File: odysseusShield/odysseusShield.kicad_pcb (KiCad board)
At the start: 2 copper layers, 53.3 x 49.5 mm, 6 parts, among them J1 Conn_01x32, J2 Conn_01x07, Q1 SSM3K333R, Q2 SSM3K333R

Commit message: working on adding logo to PCB, edited PCB based on joystick and fan additions
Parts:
- added J3: Conn_01x07, odysseusWindows:Header_P2.54mm_7, F.Cu at (156.2, 106.7)
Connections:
- J1 pad 22: Net-(J1-Pad22) -> /Joy3
- J1 pad 23: Net-(J1-Pad23) -> /Joy2
- J1 pad 24: Net-(J1-Pad24) -> /Joy1
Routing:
- net /Joy1: track 0.00 -> 43.3 mm
- net /Joy3: track 0.00 -> 41.1 mm
- net /Joy2: track 0.00 -> 40.1 mm
- net +12V: track 22.4 -> 39.7 mm
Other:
- net class Default: clearance 0.254 -> 0.1524; via_dia 0.6 -> 0.6096; via_drill 0.4 -> 0.3048
- rule trace_clearance: 0.254 -> 0.1524
- rule trace_min: 0.2 -> 0.254
- rule via_min_drill: 0.3 -> 0.3048
- rule via_min_size: 0.4 -> 0.6096
- board text added: "Alex Chapman Anil Patel Lucky Jordan (PCB Designer) Nathan Lepore Sean Szymanski Odysseus Shield V1 11/17/2017 Olin College of Engineering POE"

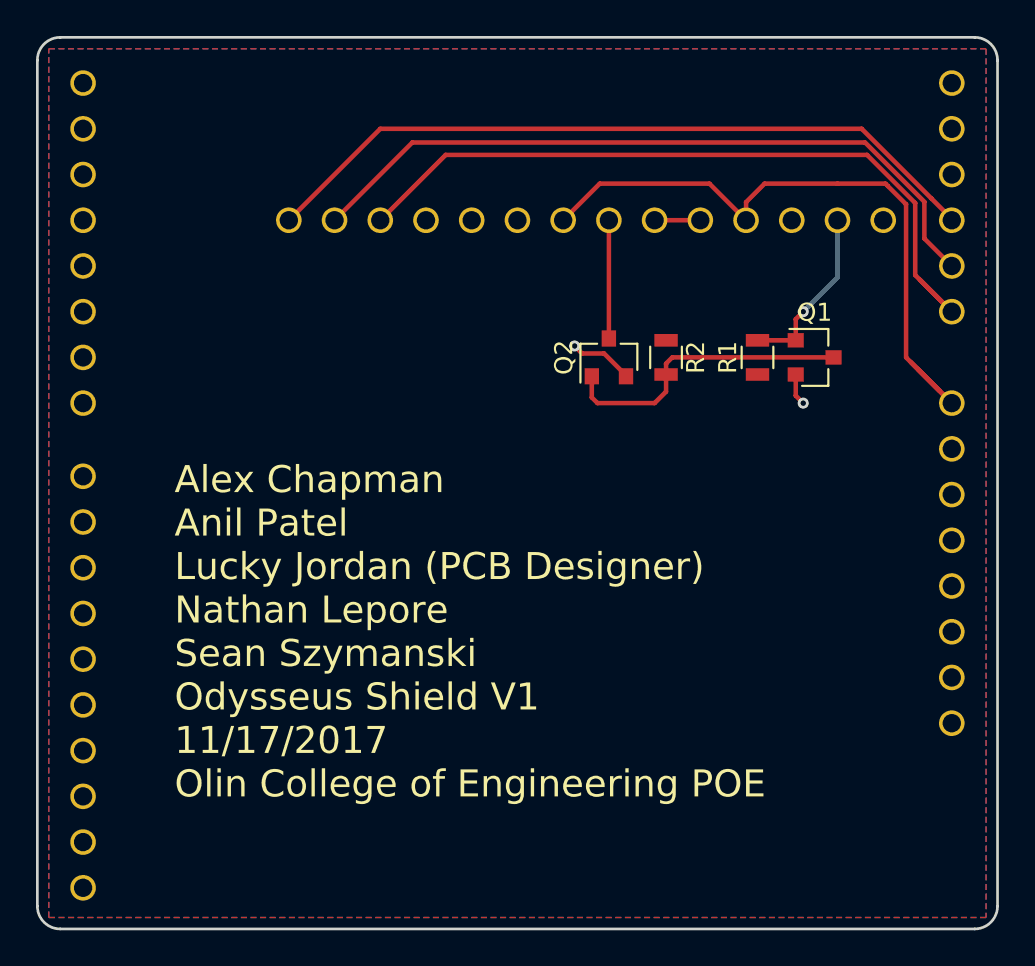
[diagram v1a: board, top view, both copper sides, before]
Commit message: finished PCB silkscreen, exported gerbers and confirmed on oshpark, ready to be ordered on pcbway
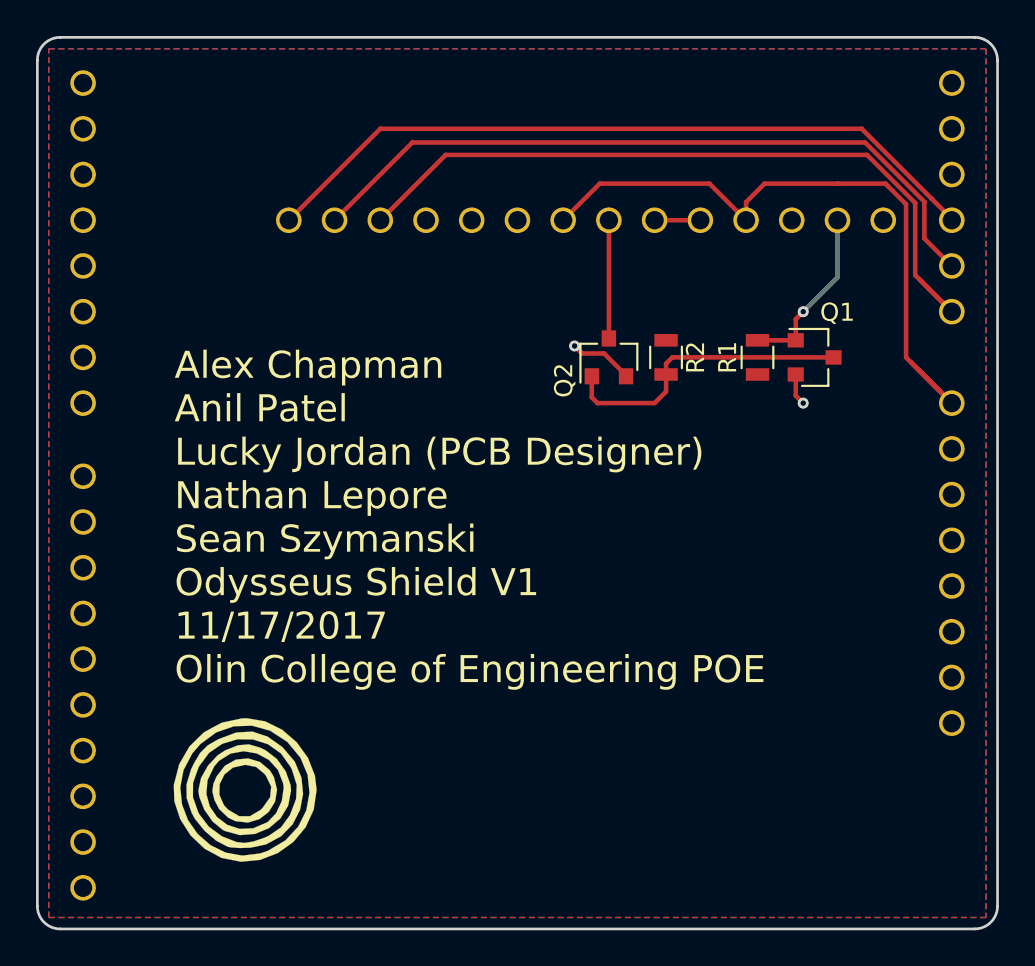
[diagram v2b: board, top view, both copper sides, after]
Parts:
- added G***: LOGO, odysseusWindows:o_logo_0.4, F.Cu at (153.7, 138.4)
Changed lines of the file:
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@@
 (kicad_pcb (version 4) (host pcbnew 4.0.7)
   (general
-    (links 21)
+    (links 0)
     (no_connects 0)
-    (area 140.079981 96.444999 195.655001 146.125001)
+    (area 142.164999 96.444999 195.655001 146.125001)
     (thickness 1.6)
     (drawings 9)
     (tracks 58)
     (zones 0)
-    (modules 7)
+    (modules 8)
     (nets 36)
   )
@@
     (tags SOT-23)
     (attr smd)
-    (fp_text reference Q2 (at 0 -2.5 90) (layer F.SilkS)
+    (fp_text reference Q2 (at -1.27 -2.5 90) (layer F.SilkS)
       (effects (font (size 1 1) (thickness 0.15)))
     )
@@
     (tags SOT-23)
     (attr smd)
-    (fp_text reference Q1 (at 0 -2.5) (layer F.SilkS)
+    (fp_text reference Q1 (at 1.27 -2.5) (layer F.SilkS)
       (effects (font (size 1 1) (thickness 0.15)))
     )
@@
       (net 22 +12V))
   )
-  (gr_text "Alex Chapman\nAnil Patel\nLucky Jordan (PCB Designer)\nNathan Lepore\nSean Szymanski\nOdysseus Shield V1\n11/17/2017\nOlin College of Engineering POE" (at 149.86 129.54) (layer F.SilkS)
+  (module odysseusWindows:o_logo_0.4 (layer F.Cu)
+    (at 153.67 138.43)
+    (fp_text reference G*** (at 0 0) (layer F.SilkS) hide
+      (effects (font (thickness 0.3)))
+    )
+    (fp_text value LOGO (at 0.75 0) (layer F.SilkS) hide
+      (effects (font (thickness 0.3)))
+    )
+    (fp_poly (pts (xy 1.222678 -3.914319) (xy 2.164503 -3.449333) (xy 2.978903 -2.749477) (xy 3.607435 -1.874859)
+      (xy 3.991653 -0.885588) (xy 4.084324 -0.101576) (xy 3.921127 0.997046) (xy 3.471579 1.973336)
+      (xy 2.789501 2.788882) (xy 1.928716 3.405271) (xy 0.943044 3.78409) (xy -0.113695 3.886926)
+      (xy -1.187679 3.675366) (xy -1.200926 3.670589) (xy -2.1331 3.166917) (xy -2.913599 2.426134)
+      (xy -3.491865 1.525204) (xy -3.817337 0.54109) (xy -3.846267 -0.235793) (xy -3.49032 -0.235793)
+      (xy -3.393106 0.703929) (xy -3.057555 1.580534) (xy -2.519127 2.348548) (xy -1.813284 2.962496)
+      (xy -0.975484 3.376903) (xy -0.041187 3.546294) (xy 0.954146 3.425193) (xy 1.382279 3.276591)
+      (xy 2.348398 2.704415) (xy 3.061839 1.937307) (xy 3.51237 1.034627) (xy 3.68976 0.055738)
+      (xy 3.583778 -0.939997) (xy 3.184194 -1.893217) (xy 2.480776 -2.744559) (xy 2.428118 -2.791602)
+      (xy 1.500704 -3.392495) (xy 0.498408 -3.671625) (xy -0.520185 -3.636451) (xy -1.496487 -3.294427)
+      (xy -2.37191 -2.653009) (xy -2.827901 -2.122685) (xy -3.313739 -1.193156) (xy -3.49032 -0.235793)
+      (xy -3.846267 -0.235793) (xy -3.851021 -0.363436) (xy -3.552371 -1.524398) (xy -2.978662 -2.51839)
+      (xy -2.1761 -3.303093) (xy -1.190897 -3.836188) (xy -0.069261 -4.075354) (xy 0.211872 -4.084325)
+      (xy 1.222678 -3.914319)) (layer F.SilkS) (width 0.01))
+    (fp_poly (pts (xy 1.364203 -3.063673) (xy 2.195535 -2.471387) (xy 2.866895 -1.678515) (xy 3.239426 -0.794989)
+      (xy 3.331774 0.120389) (xy 3.162584 1.008819) (xy 2.750501 1.811498) (xy 2.114169 2.469626)
+      (xy 1.272236 2.924401) (xy 0.427129 3.105611) (xy -0.17625 3.12586) (xy -0.691043 3.089177)
+      (xy -0.844975 3.056091) (xy -1.48615 2.72289) (xy -2.133861 2.172726) (xy -2.665934 1.519748)
+      (xy -2.856842 1.176389) (xy -3.132221 0.355733) (xy -3.133185 0.302588) (xy -2.786773 0.302588)
+      (xy -2.489731 1.140074) (xy -2.43294 1.250457) (xy -1.904037 1.937762) (xy -1.175283 2.476281)
+      (xy -0.364796 2.791182) (xy 0.079112 2.841958) (xy 0.575885 2.760565) (xy 1.181128 2.555207)
+      (xy 1.427749 2.442307) (xy 2.106031 1.978859) (xy 2.58081 1.325812) (xy 2.61993 1.250125)
+      (xy 2.944395 0.396702) (xy 2.977702 -0.381071) (xy 2.721382 -1.208865) (xy 2.651733 -1.358202)
+      (xy 2.105268 -2.127771) (xy 1.380839 -2.643303) (xy 0.548805 -2.904799) (xy -0.320475 -2.912258)
+      (xy -1.15664 -2.665681) (xy -1.889334 -2.165068) (xy -2.448195 -1.410418) (xy -2.47411 -1.358202)
+      (xy -2.780946 -0.490907) (xy -2.786773 0.302588) (xy -3.133185 0.302588) (xy -3.146046 -0.406046)
+      (xy -2.89322 -1.230656) (xy -2.742543 -1.553123) (xy -2.379621 -2.168076) (xy -1.953752 -2.584315)
+      (xy -1.3755 -2.920166) (xy -0.37771 -3.293767) (xy 0.516083 -3.344046) (xy 1.364203 -3.063673)) (layer F.SilkS) (width 0.01))
+    (fp_poly (pts (xy 0.934292 -2.455531) (xy 1.248043 -2.306701) (xy 1.875302 -1.822399) (xy 2.365473 -1.137932)
+      (xy 2.636036 -0.383136) (xy 2.664336 -0.078326) (xy 2.504806 0.77094) (xy 2.072031 1.48407)
+      (xy 1.434731 2.021144) (xy 0.66163 2.342242) (xy -0.178552 2.407444) (xy -1.017094 2.17683)
+      (xy -1.12388 2.122239) (xy -1.686037 1.660195) (xy -2.152899 0.998327) (xy -2.436671 0.278731)
+      (xy -2.458022 0.114053) (xy -2.042971 0.114053) (xy -1.852398 0.813531) (xy -1.449583 1.403493)
+      (xy -0.881235 1.835131) (xy -0.194057 2.059636) (xy 0.565243 2.0282) (xy 1.34996 1.692013)
+      (xy 1.365791 1.681715) (xy 1.835134 1.190875) (xy 2.151805 0.506966) (xy 2.255104 -0.219947)
+      (xy 2.229993 -0.454751) (xy 1.935655 -1.213054) (xy 1.421236 -1.778029) (xy 0.762006 -2.130744)
+      (xy 0.03323 -2.252268) (xy -0.689822 -2.123671) (xy -1.331885 -1.72602) (xy -1.600573 -1.41821)
+      (xy -1.974599 -0.64613) (xy -2.042971 0.114053) (xy -2.458022 0.114053) (xy -2.482812 -0.077138)
+      (xy -2.34043 -0.755671) (xy -1.954397 -1.449143) (xy -1.40783 -2.033129) (xy -0.998978 -2.298415)
+      (xy -0.282432 -2.582375) (xy 0.312834 -2.634566) (xy 0.934292 -2.455531)) (layer F.SilkS) (width 0.01))
+    (fp_poly (pts (xy 0.931228 -1.658915) (xy 1.482273 -1.19522) (xy 1.709564 -0.827863) (xy 1.888566 -0.109637)
+      (xy 1.773502 0.557401) (xy 1.424634 1.119263) (xy 0.902221 1.521959) (xy 0.266526 1.711501)
+      (xy -0.422191 1.633903) (xy -0.825394 1.443218) (xy -1.3337 0.953275) (xy -1.594413 0.456746)
+      (xy -1.662163 0.167423) (xy -1.319452 0.167423) (xy -1.061208 0.748488) (xy -0.82492 0.999941)
+      (xy -0.216569 1.356172) (xy 0.377266 1.358662) (xy 0.968358 1.006806) (xy 1.079398 0.901775)
+      (xy 1.4975 0.309891) (xy 1.561142 -0.282539) (xy 1.27093 -0.887285) (xy 1.177564 -1.002543)
+      (xy 0.723321 -1.37759) (xy 0.155371 -1.491628) (xy 0.107883 -1.492028) (xy -0.554684 -1.346028)
+      (xy -1.034533 -0.964405) (xy -1.300008 -0.431732) (xy -1.319452 0.167423) (xy -1.662163 0.167423)
+      (xy -1.708365 -0.029879) (xy -1.649244 -0.44787) (xy -1.479508 -0.841336) (xy -1.01414 -1.447296)
+      (xy -0.401128 -1.785309) (xy 0.275378 -1.85573) (xy 0.931228 -1.658915)) (layer F.SilkS) (width 0.01))
+  )
+  (gr_text "Alex Chapman\nAnil Patel\nLucky Jordan (PCB Designer)\nNathan Lepore\nSean Szymanski\nOdysseus Shield V1\n11/17/2017\nOlin College of Engineering POE" (at 149.86 123.19) (layer F.SilkS)
     (effects (font (size 1.5 1.5) (thickness 0.3)) (justify left))
   )

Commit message: added labels to pins and indicator leds
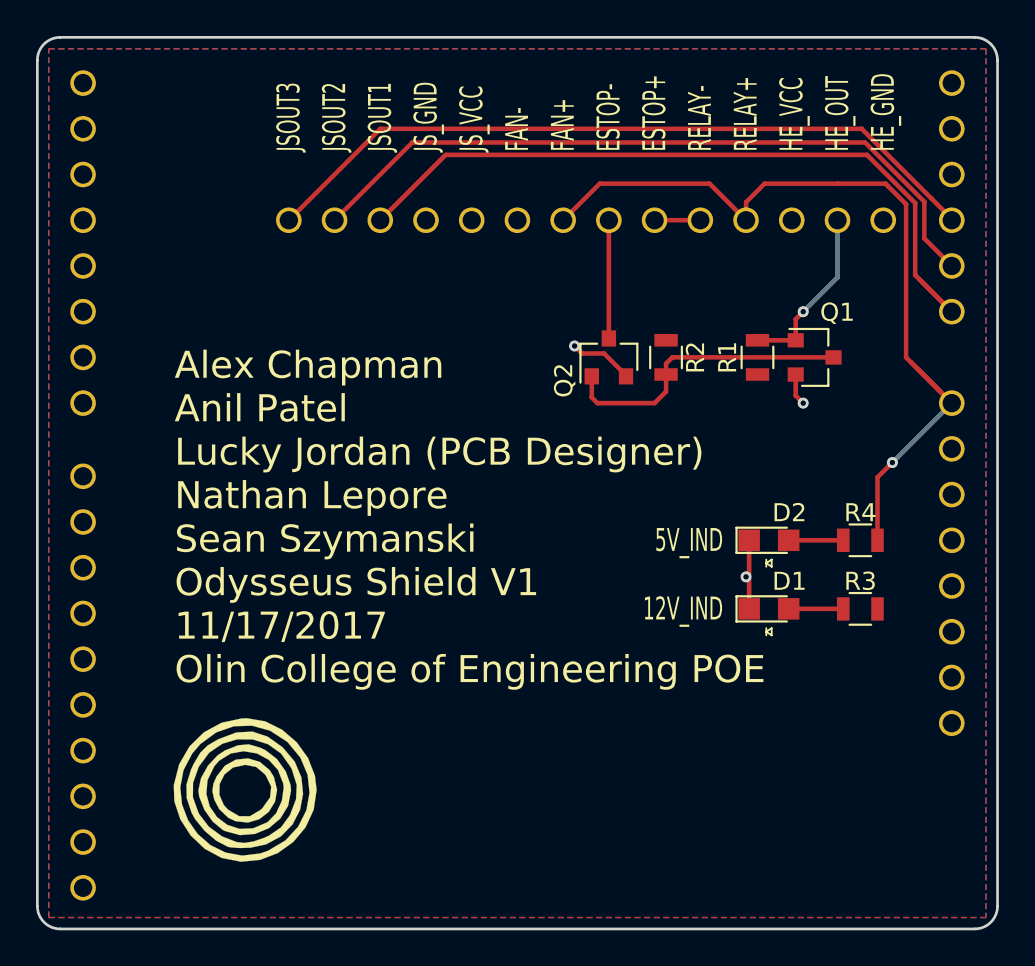
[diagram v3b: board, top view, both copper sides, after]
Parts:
- added D1: LED_0805, footprints:LED_0805_OEM, F.Cu at (182.9, 128.3)
- added D2: LED_0805, footprints:LED_0805_OEM, F.Cu at (182.9, 124.5)
- added R3: R_200, footprints:R_0805_OEM, F.Cu at (188.0, 128.3)
- added R4: R_1k, footprints:R_0805_OEM, F.Cu at (188.0, 124.5)
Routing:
- net +12V: track 39.7 -> 49.0 mm, vias 0 -> 1
- net GND: track 5.34 -> 9.29 mm, vias 2 -> 3
- net Net-(D2-Pad2): track 0.00 -> 3.03 mm
- net Net-(D1-Pad2): track 0.00 -> 3.03 mm
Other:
- board text added: "12V_IND"
- board text added: "5V_IND"
- board text added: "ESTOP+"
- board text added: "ESTOP-"
- board text added: "FAN+"
- board text added: "FAN-"
- board text added: "HE_GND"
- board text added: "HE_OUT"
- board text added: "HE_VCC"
- board text added: "JSOUT1"
- board text added: "JSOUT2"
- board text added: "JSOUT3"
- board text added: "JS_GND"
- board text added: "JS_VCC"
- board text added: "RELAY+"
- board text added: "RELAY-"

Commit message: added some more silk screen stuff
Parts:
- added G***: LOGO, LuckyFootprints:lucky_watermelon, B.Cu at (168.9, 120.7)
- added REF***: KiCad-Logo_8mm_SilkScreen, Symbols:KiCad-Logo_8mm_SilkScreen, F.Cu at (170.2, 138.4)
- added REF***: OSHW-Logo_7.5x8mm_SilkScreen, Symbols:OSHW-Logo_7.5x8mm_SilkScreen, F.Cu at (186.7, 138.4)
